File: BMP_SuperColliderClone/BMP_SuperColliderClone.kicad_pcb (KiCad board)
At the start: 2 copper layers, 41.9 x 118 mm, 63 parts, among them J1 BARREL_JACK, Q1 MMBT3904, Q2 MMBT3904, Q3 MMBT3904, Q4 MMBT3904

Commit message: Board Layout
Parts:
- J1: footprint Connectors:BARREL_JACK -> .pretty:BARREL_JACK
- moved DEPTH1 106.7 mm to (50.4, 134.4)
- moved J_AUX2MAIN_2 91.3 mm to (40.5, 128.4)
- moved J_AUX2MAIN_1 91.3 mm to (79.1, 128.4)
- moved TONE1 89.4 mm to (74.2, 118.9)
- moved MIDS1 89.3 mm to (50.4, 118.9)
- moved SUSTAIN1 87.5 mm to (74.2, 134.4)
- moved D6 87.0 mm to (59.2, 133.0), turned to 0 degrees
- moved R26 85.5 mm to (55.2, 134.2), turned to 270 degrees
- moved VOL1 71.9 mm to (50.4, 150.2)
- moved C13 31.6 mm to (116.7, 123.2)
- moved C4 31.5 mm to (119.8, 168.7), turned to 180 degrees
- moved J_IN1 30.9 mm to (115.2, 155.7)
- moved R22 30.7 mm to (111.6, 127.1)
- moved R24 30.7 mm to (107.6, 123.1)
- moved C14 30.4 mm to (104.4, 123.1)
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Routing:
- net Net-(J_AUX2MAIN_2-Pad6): track 0.00 -> 42.2 mm
- net Net-(J_AUX2MAIN_2-Pad5): track 0.00 -> 40.5 mm, vias 0 -> 1
- net Net-(J_AUX2MAIN_2-Pad8): track 0.00 -> 40.2 mm
- net Net-(DEPTH1-Pad3): track 0.00 -> 38.4 mm, vias 0 -> 4
- net Net-(J_AUX2MAIN_2-Pad4): track 0.00 -> 37.4 mm, vias 0 -> 1
- net Net-(DEPTH1-Pad1): track 0.00 -> 35.9 mm, vias 0 -> 2
- net Net-(D6-Pad2): track 0.00 -> 28.1 mm
- net Net-(J_OUT1-Pad1): track 50.2 -> 23.2 mm
- net Net-(J_AUX2MAIN_1-Pad5): track 0.00 -> 26.7 mm
- net Net-(J_AUX2MAIN_2-Pad1): track 0.00 -> 22.8 mm, vias 0 -> 1
- net Net-(J_AUX2MAIN_1-Pad3): track 0.00 -> 17.4 mm, vias 0 -> 1
- net Net-(J_AUX2MAIN_1-Pad8): track 0.00 -> 17.3 mm
- net Net-(J_AUX2MAIN_1-Pad4): track 0.00 -> 16.7 mm
- net Net-(J_AUX2MAIN_1-Pad6): track 0.00 -> 12.6 mm
- net Net-(J_AUX2MAIN_2-Pad7): track 0.00 -> 11.1 mm
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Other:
- board size 41.9 x 118 mm -> 86.7 x 92.1 mm
- board text added: "R1"
- board text added: "SuperCollider"

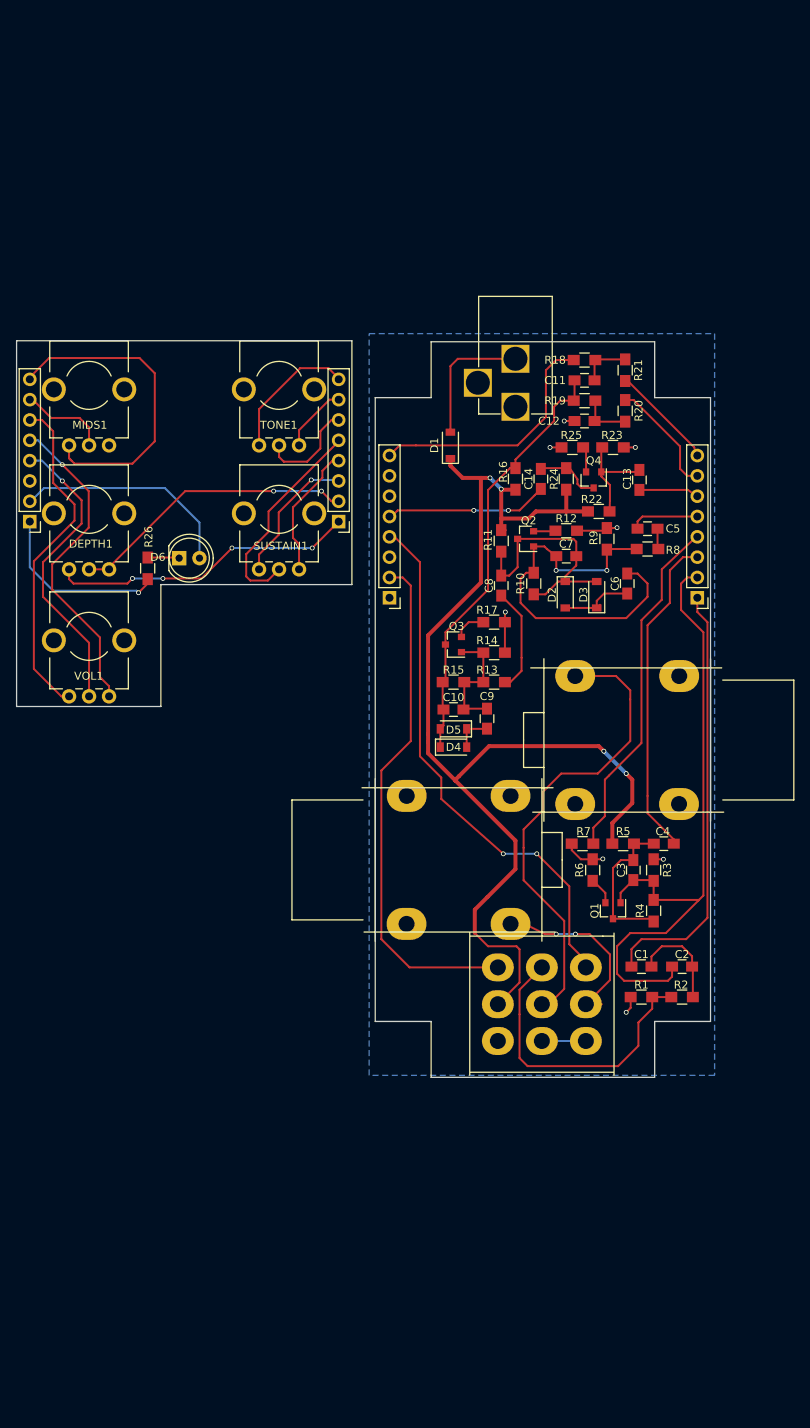
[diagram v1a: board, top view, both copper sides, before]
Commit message: Added SuperCollidfer ModPins
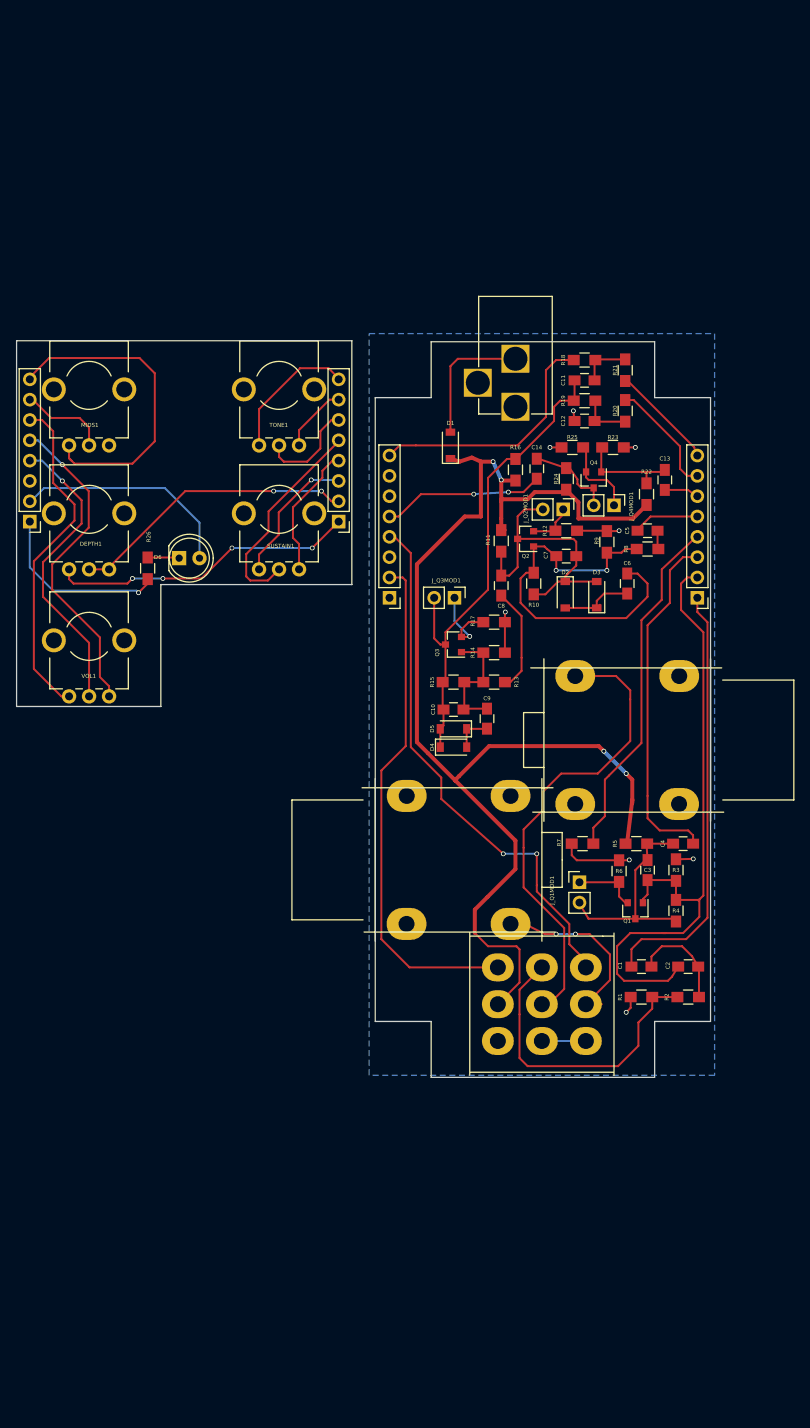
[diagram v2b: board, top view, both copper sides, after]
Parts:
- added J_Q1MOD1: CONN_01X02, Pin_Headers:Pin_Header_Straight_1x02_Pitch2.54mm, F.Cu at (109.2, 173.5)
- added J_Q2MOD1: CONN_01X02, Pin_Headers:Pin_Header_Straight_1x02_Pitch2.54mm, F.Cu at (107.2, 126.9)
- added J_Q3MOD1: CONN_01X02, Pin_Headers:Pin_Header_Straight_1x02_Pitch2.54mm, F.Cu at (93.6, 137.9)
- added J_Q4MOD1: CONN_01X02, Pin_Headers:Pin_Header_Straight_1x02_Pitch2.54mm, F.Cu at (113.5, 126.4)
- moved R22 6.35 mm to (117.6, 125.0), turned to 90 degrees
- moved R6 3.30 mm to (114.2, 172.1)
- moved C13 3.18 mm to (119.9, 123.2)
- moved Q1 2.79 mm to (116.2, 177.0)
- moved R3 2.79 mm to (121.3, 172.0)
- moved R4 2.79 mm to (121.3, 177.0)
- moved C4 2.41 mm to (122.2, 168.7)
- moved C3 1.78 mm to (117.7, 172.0)
- moved R5 1.65 mm to (116.3, 168.7)
- moved C14 1.37 mm to (103.9, 121.8)
- moved R16 1.14 mm to (101.2, 121.9)
- moved C2 0.76 mm to (122.8, 184.0)
- moved R2 0.76 mm to (122.8, 187.8)
- moved R9 0.38 mm to (112.6, 130.9)
- moved C5 0.25 mm to (117.7, 129.5)
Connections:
- net Net-(C10-Pad1) renamed /Q3_CMOD
- net Net-(C14-Pad1) renamed /Q4_CMOD
- net Net-(C3-Pad1) renamed /Q1_CMOD
- net Net-(C7-Pad1) renamed /Q2_CMOD
- net Net-(Q1-Pad2) renamed /Q1_EMOD
- net Net-(Q2-Pad2) renamed /Q2_EMOD
- net Net-(Q3-Pad2) renamed /Q3_EMOD
- net Net-(Q4-Pad2) renamed /Q4_EMOD
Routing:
- net /+9V: track 146.2 -> 158.7 mm
- net /Q1_CMOD: track 19.1 -> 26.9 mm
- net /Q3_CMOD: track 54.6 -> 61.7 mm
- net /Q4_EMOD: track 3.22 -> 10.2 mm
- net /Q3_EMOD: track 4.14 -> 10.6 mm, vias 0 -> 1
- net /Q2_CMOD: track 30.7 -> 37.0 mm
- net /GND: track 23.2 -> 28.5 mm
- net /Q1_EMOD: track 3.44 -> 8.62 mm
- net /SUS_P3: track 41.7 -> 45.3 mm
- net /TONE_P2: track 7.37 -> 4.20 mm
- net /Q2_EMOD: track 2.76 -> 5.83 mm
- net /Q4_CMOD: track 8.75 -> 11.6 mm
- net Net-(R1-Pad1): track 38.0 -> 38.8 mm
- net Net-(C13-Pad1): track 13.5 -> 12.9 mm
- net /LED_AN: track 64.8 -> 64.3 mm

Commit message: Added THT diodes to supercollider
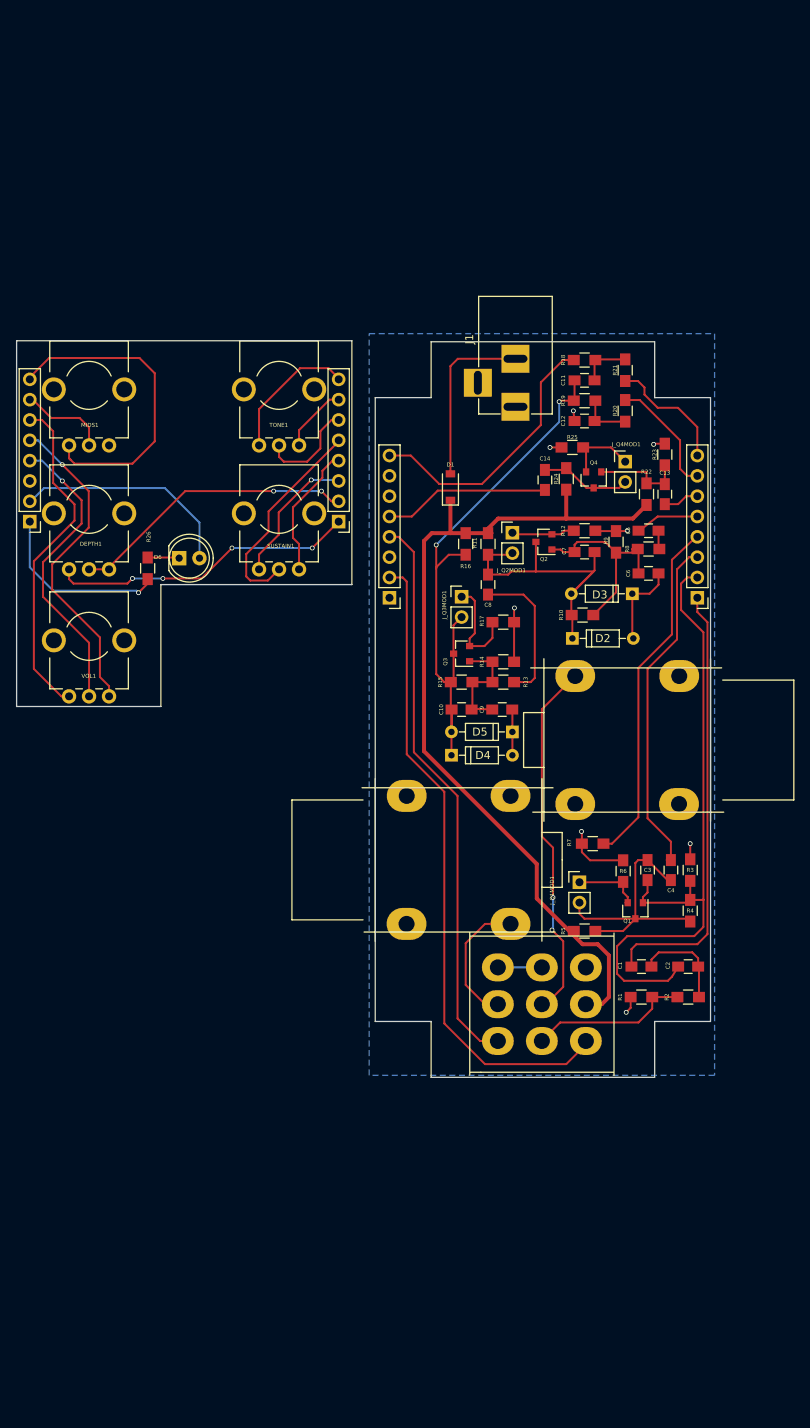
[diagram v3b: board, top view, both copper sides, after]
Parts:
- D2, D3, D4, D5: footprint Diodes_SMD:D_SOD-123 -> Diodes_THT:D_DO-35_SOD27_P7.62mm_Horizontal
- J1: footprint .pretty:BARREL_JACK -> Connectors:BARREL_JACK
- moved R5 12.7 mm to (109.9, 179.6)
- moved R16 11.2 mm to (95.0, 131.2), turned to 270 degrees
- moved D5 7.38 mm to (100.8, 154.7)
- moved R10 7.26 mm to (109.6, 140.1), turned to 0 degrees
- moved J_Q2MOD1 6.99 mm to (100.8, 129.8), turned to 0 degrees
- moved R23 6.54 mm to (119.9, 120.0), turned to 90 degrees
- moved J_Q4MOD1 5.64 mm to (114.9, 120.9), turned to 0 degrees
- moved D2 5.53 mm to (108.3, 143.0), turned to 0 degrees
- moved D1 5.21 mm to (93.1, 124.1)
- moved D3 4.45 mm to (115.8, 137.4), turned to 180 degrees
- moved C4 3.64 mm to (120.7, 172.0), turned to 270 degrees
- moved C6 2.95 mm to (117.9, 134.9), turned to 180 degrees
- moved C7 2.34 mm to (109.9, 132.2)
- moved Q2 2.32 mm to (104.8, 130.9)
- moved R12 2.29 mm to (109.9, 129.5)
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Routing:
- net /+9V: track 158.7 -> 110.7 mm, vias 4 -> 0
- net Net-(C6-Pad2): track 48.5 -> 25.4 mm, vias 2 -> 0
- net Net-(R1-Pad1): track 38.8 -> 20.2 mm
- net /LED_AN: track 64.3 -> 80.8 mm
- net Net-(J_IN1-Pad1): track 59.7 -> 47.1 mm, vias 0 -> 2
- net /Q3_CMOD: track 61.7 -> 73.1 mm, vias 0 -> 2
- net /Q1_CMOD: track 26.9 -> 34.3 mm
- net Net-(C8-Pad2): track 13.1 -> 18.9 mm
- net Net-(D1-Pad2): track 17.1 -> 22.4 mm
- net /VOL_P2: track 67.1 -> 71.2 mm, vias 2 -> 0
- net Net-(J_OUT1-Pad1): track 23.2 -> 19.4 mm, vias 2 -> 0
- net /Q2_CMOD: track 37.0 -> 40.3 mm
- net /Q3_EMOD: track 10.6 -> 13.8 mm, vias 1 -> 0
- net /TONE_P3: track 13.1 -> 15.8 mm
- net /MIDS_P3: track 31.5 -> 34.2 mm
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
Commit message: SuperCollider
Tidy up board layout
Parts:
- moved R23 2.37 mm to (117.6, 119.4)
- moved R13 0.51 mm to (99.7, 149.0)
- moved R15 0.51 mm to (94.5, 149.0)
- moved R8 0.51 mm to (117.9, 132.3)
- moved D2 0.51 mm to (108.3, 143.5)
- moved C12 0.38 mm to (109.9, 116.2)
- moved R10 0.38 mm to (109.6, 140.5)
- moved R20 0.38 mm to (114.9, 114.9)
- moved R19 0.25 mm to (109.9, 113.5)
- moved C11 0.13 mm to (109.9, 110.9)
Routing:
- net /TONE_P3: track 15.8 -> 13.4 mm
- net /+9V: track 110.7 -> 112.7 mm
- net Net-(C13-Pad1): track 12.4 -> 14.3 mm
- net /GND: track 27.9 -> 29.3 mm
- net /SUS_P2: track 7.98 -> 8.89 mm
- net /TONE_P1: track 15.1 -> 14.2 mm
- net Net-(C5-Pad2): track 2.33 -> 2.84 mm
- net /Q2_CMOD: track 40.3 -> 40.8 mm
- net Net-(C6-Pad1): track 10.8 -> 11.3 mm

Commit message: Added documentation
- Schema (PDF, SVG(
- Board Layout (PDF/SVG)
- BOM (XML)
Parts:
- moved MIDS1 9.40 mm to (50.5, 128.3)
- moved TONE1 9.40 mm to (74.3, 128.3)
- moved D6 9.40 mm to (59.3, 142.4)
- moved DEPTH1 9.40 mm to (50.5, 143.8)
- moved J_AUX2MAIN_1 9.40 mm to (79.2, 137.8)
- moved J_AUX2MAIN_2 9.40 mm to (40.6, 137.8)
- moved R26 9.40 mm to (55.4, 143.6)
- moved SUSTAIN1 9.40 mm to (74.3, 143.8)
- moved VOL1 9.40 mm to (50.5, 159.6)
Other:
- board size 86.7 x 92.1 mm -> 86.6 x 91.9 mm

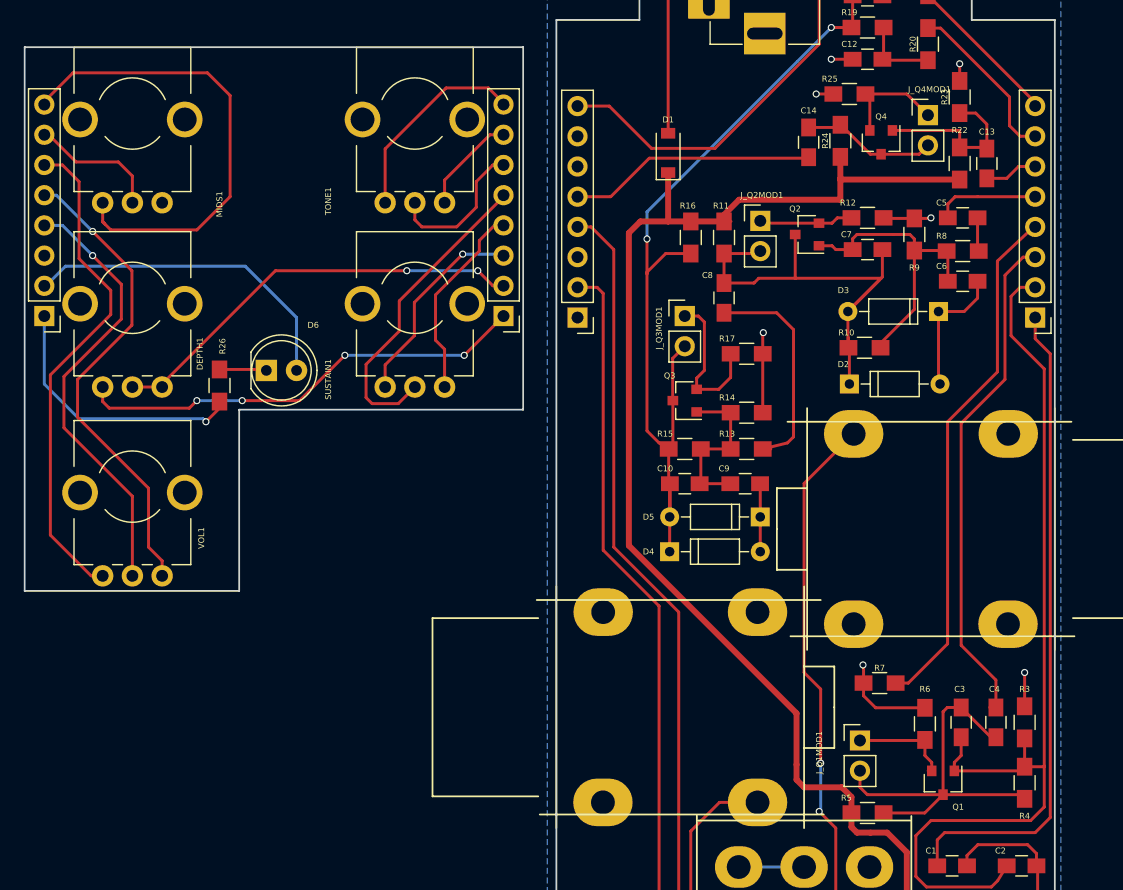
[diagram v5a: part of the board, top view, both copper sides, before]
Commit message: updated supercollider
- reversed polarity for sustain and depth pots
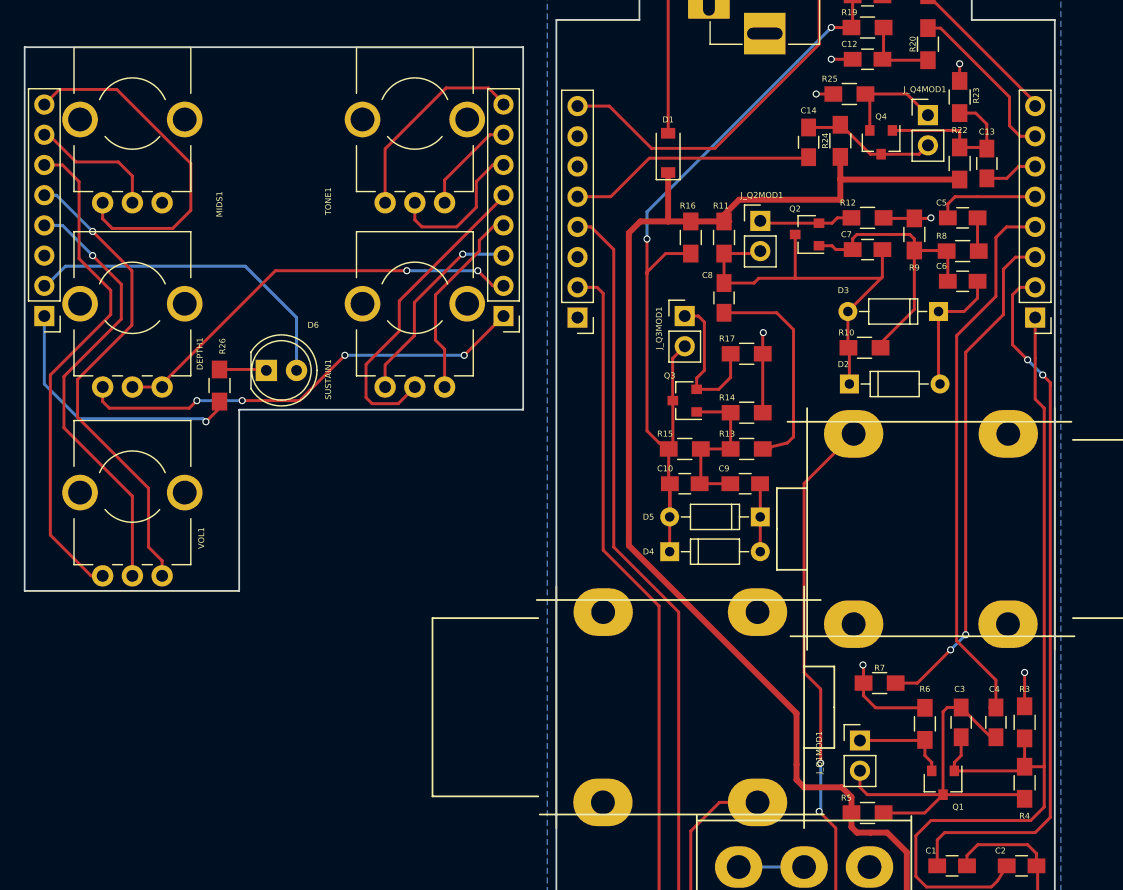
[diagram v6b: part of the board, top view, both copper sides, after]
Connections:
- C1 pad 2: /DEPTH_P3 -> /DEPTH_P1_2
- C2 pad 2: /DEPTH_P1_2 -> /DEPTH_P3
- C3 pad 2: /DEPTH_P1_2 -> /DEPTH_P3
- C4 pad 1: /SUS_P3 -> /SUS_P1
- Q1 pad 1: /DEPTH_P1_2 -> /DEPTH_P3
- R3 pad 2: /DEPTH_P1_2 -> /DEPTH_P3
- R4 pad 2: /DEPTH_P1_2 -> /DEPTH_P3
- R7 pad 1: /SUS_P1 -> /SUS_P3
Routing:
- net /DEPTH_P1_2: track 83.9 -> 59.9 mm, vias 0 -> 2
- net /DEPTH_P3: track 55.0 -> 79.0 mm
- net Net-(J_AUX2MAIN_2-Pad8): track 40.2 -> 29.3 mm
- net /Q2_CMOD: track 40.8 -> 36.6 mm
- net /SUS_P1: track 43.8 -> 47.0 mm
- net /SUS_P3: track 43.2 -> 42.7 mm, vias 0 -> 2
